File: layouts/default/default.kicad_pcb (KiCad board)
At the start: 2 copper layers, 37 x 37 mm, 104 parts, among them U1 TI_RPE0009B_VQFN-HR-9_2x2mm_P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, U6 TI_RPE0009B_VQFN-HR-9_2x2mm_P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

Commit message: REV-009b: Align buck design with Brave F7 dual-5V topology
Both bucks now use LMR43620MB5RPER (fixed 5V) matching the Brave F7
reference board (both marked "2MB5"). Second buck provides dedicated
clean 5V for VTX instead of 10V — removes RT resistor, FB divider.

Additional changes:
- Add EN/UVLO dividers (430k/100k) on both bucks for production-grade
  under-voltage lockout at ~6.5V rising
- Add PGOOD pullup resistors (100k) on both bucks
- Switch inductors from 4.7uH/6.3mm to 2.2uH/4mm (Wuerth MAPI-4020)
  matching TI 1MHz recommendation and Brave F7 inductor specs
- Unhide all reference designators on PCB silkscreen

Co-Authored-By: Claude Opus 4.6 <noreply@anthropic.com>
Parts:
- removed R28, R29: , Resistor_SMD:R_0402_1005Metric
- added R14: , Resistor_SMD:R_0402_1005Metric, F.Cu at (0.00, -90.0)
- added R15: , Resistor_SMD:R_0402_1005Metric, F.Cu at (0.00, -100.0)
- added R16: , Resistor_SMD:R_0402_1005Metric, F.Cu at (0.00, -20.0)
- added R27: , Resistor_SMD:R_0402_1005Metric, F.Cu at (0.00, -30.0)
- added R30: , Resistor_SMD:R_0402_1005Metric, F.Cu at (0.00, 0.00)
- C25, C26, C33, C39, C40, C43: moved to B.Cu
- C27: footprint Capacitor_SMD:C_1206_3216Metric -> Capacitor_SMD:C_0805_2012Metric
- C28: footprint Capacitor_SMD:C_1206_3216Metric -> Capacitor_SMD:C_0402_1005Metric
- C37: footprint Capacitor_SMD:C_0402_1005Metric -> Capacitor_SMD:C_1206_3216Metric
- C38: footprint Capacitor_SMD:C_0805_2012Metric -> Capacitor_SMD:C_1206_3216Metric
- L1: footprint Inductor_SMD:L_6.3x6.3_H3 -> Inductor_SMD:L_Wuerth_MAPI-4020; moved to B.Cu
- L2: footprint Inductor_SMD:L_6.3x6.3_H3 -> Inductor_SMD:L_Wuerth_MAPI-4020
- U1: value TI_RPE0009B_VQFN-HR-9_2x2mm_P0.5mm -> (none)
- U6: value TI_RPE0009B_VQFN-HR-9_2x2mm_P0.5mm -> (none); moved to B.Cu
- moved C43 227.9 mm to (163.6, 98.7)
- moved C40 224.1 mm to (164.1, 102.7)
- moved C33 213.8 mm to (174.3, 93.7)
- moved C39 210.2 mm to (158.3, 98.3)
- moved C37 189.5 mm to (0.00, -40.0)
- moved C38 189.5 mm to (0.00, -50.0)
- moved L2 170.7 mm to (0.00, -70.0)
- moved U1 161.4 mm to (0.00, 0.00)
- moved Q4 98.3 mm to (158.8, 59.4)
- moved R31 96.6 mm to (159.0, 34.8)
- moved C26 73.4 mm to (168.2, 97.1)
- moved U6 55.5 mm to (171.6, 106.2), turned to -90 degrees
- moved C25 43.3 mm to (169.9, 93.0)
- moved L1 35.9 mm to (163.2, 92.1)
- moved C24 10.0 mm to (0.00, -10.0)
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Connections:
- net buck_10v-vcc renamed buck_vtx-vcc
- net vtx_10v renamed vtx_5v
- C24 pad 1: vbat -> buck_vtx-boot
- C24 pad 2: baro-gnd -> buck_vtx-sw
- C27 pad 1: rail_10v -> vbat
- C28 pad 1: rail_10v -> vbat
- C37 pad 1: buck_10v-boot -> rail_5v_vtx
- C37 pad 2: buck_10v-sw -> baro-gnd
- C38 pad 1: vbat -> rail_5v_vtx
- L2 pad 1: buck_10v-sw -> buck_vtx-sw
- L2 pad 2: rail_10v -> rail_5v_vtx
- Q2 pad 2: rail_10v -> rail_5v_vtx
- R12 pad 1: rt -> buck_vtx-en
- R31 pad 2: rail_10v -> rail_5v_vtx
- U1 pad 1: rt -> baro-gnd
- U1 pad 2: buck_10v-pgood -> buck_vtx-pgood
- U1 pad 3: vbat -> buck_vtx-en
- U1 pad 5: buck_10v-sw -> buck_vtx-sw
- U1 pad 6: buck_10v-boot -> buck_vtx-boot
- U1 pad 8: fb -> rail_5v_vtx
- U6 pad 3: vbat -> buck-en

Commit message: Replace USB-C connector with HRO TYPE-C-31-M-12
Swap GCT USB4085-GF-A (16-pin full SMD) for HRO TYPE-C-31-M-12
(12-pin, 4 THT mounting tabs + SMD signal pads) to match Brave F7
form factor. Identical pin names — no wiring changes needed.
Unhide all reference designators on PCB silkscreen.

Co-Authored-By: Claude Opus 4.6 <noreply@anthropic.com>
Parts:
- C24, C27, C28, C37, C38, C44, L2, R12, R14, R15, R16, R27, R30, U1: moved to B.Cu
- J6: footprint Connector_USB:USB_C_Receptacle_GCT_USB4085 -> Connector_USB:USB_C_Receptacle_HRO_TYPE-C-31-M-12
- moved R15 238.6 mm to (123.1, 104.4), turned to 180 degrees
- moved R14 230.2 mm to (124.8, 103.5), turned to 180 degrees
- moved R12 220.8 mm to (122.9, 103.5), turned to 180 degrees
- moved L2 220.1 mm to (127.8, 109.2)
- moved C44 208.4 mm to (122.7, 108.5), turned to 180 degrees
- moved C38 206.1 mm to (132.4, 108.0)
- moved C37 200.3 mm to (132.4, 110.3)
- moved C28 183.9 mm to (125.5, 104.4)
- moved R27 182.4 mm to (119.2, 108.1), turned to 180 degrees
- moved C27 179.0 mm to (127.2, 105.9)
- moved R16 173.7 mm to (117.3, 108.1), turned to 180 degrees
- moved C24 171.9 mm to (124.5, 108.5)
- moved U1 163.4 mm to (124.0, 106.4), turned to -90 degrees
- moved R30 160.4 mm to (117.7, 109.0), turned to 180 degrees
- moved C33 56.4 mm to (120.0, 109.0)
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
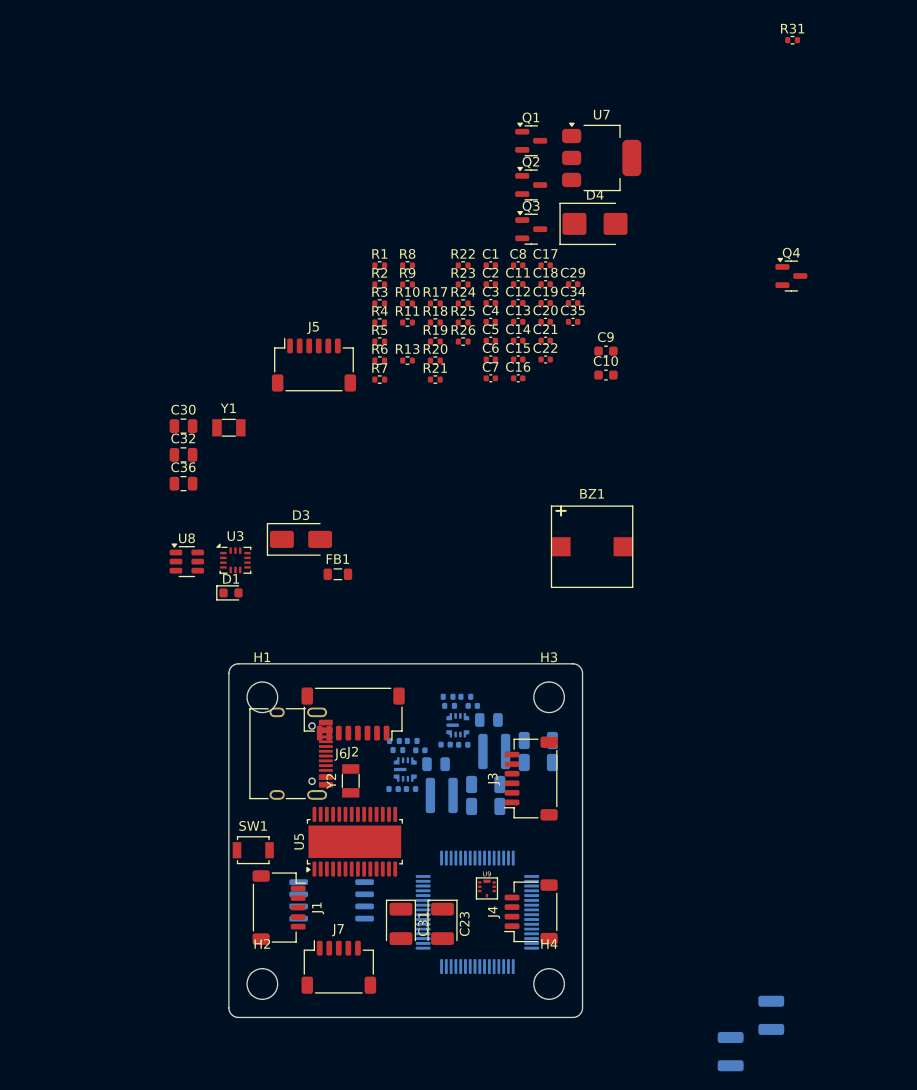
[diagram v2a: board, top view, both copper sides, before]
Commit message: Update tantalum caps from 22µF to 47µF to match Brave F7
C31 (LDO output) and C23 (3.3V bulk) changed from TAJB226K010RNJ
to TAJB476K010RNJ. Same Case B footprint. Marking "476A" matches
Brave F7 reference board. Also marks Groups 2 and 3 as placed.

Co-Authored-By: Claude Opus 4.6 <noreply@anthropic.com>
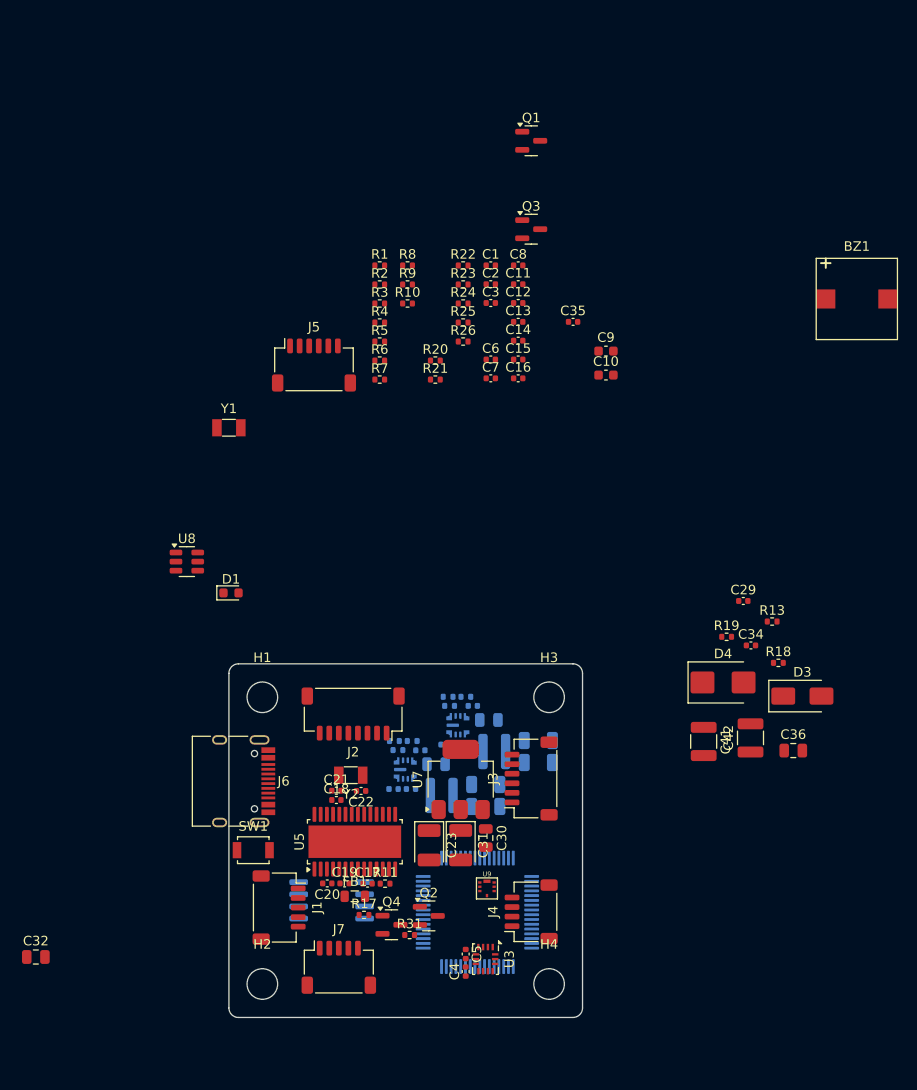
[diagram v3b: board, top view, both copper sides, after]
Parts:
- C41, C42: moved to F.Cu
- moved R31 101.8 mm to (118.9, 128.4)
- moved Q4 79.7 mm to (117.0, 127.3)
- moved Q2 77.2 mm to (120.9, 126.4)
- moved C36 69.6 mm to (159.1, 109.1)
- moved C4 68.0 mm to (124.8, 132.2), turned to 90 degrees
- moved C17 67.3 mm to (114.5, 123.0)
- moved U7 66.7 mm to (124.2, 112.1), turned to 90 degrees
- moved R17 64.4 mm to (114.1, 126.3)
- moved C19 64.3 mm to (112.1, 123.0)
- moved C5 64.2 mm to (124.8, 130.4), turned to -90 degrees
- moved C20 63.0 mm to (110.3, 123.0), turned to 180 degrees
- moved R11 58.8 mm to (116.3, 123.0)
- moved C18 58.2 mm to (111.2, 114.2)
- moved D3 55.0 mm to (160.0, 103.4)
- moved C32 54.8 mm to (79.8, 130.7)
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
